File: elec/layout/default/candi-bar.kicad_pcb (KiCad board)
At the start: 2 copper layers, 85 x 25 mm, 25 parts, among them J1 ?, J10 ?, J11 ?, J12 ?, J13 ?, J14 ?, J15 ?, J16 ?, J2 ?, J3 ?, J4 ?, J5 ?, J6 ?, J7 ?, J8 ?, J9 ?, U1 ?, U2 ?, U3 ?, U4 ?, U5 ?, U6 ?, U7 ?

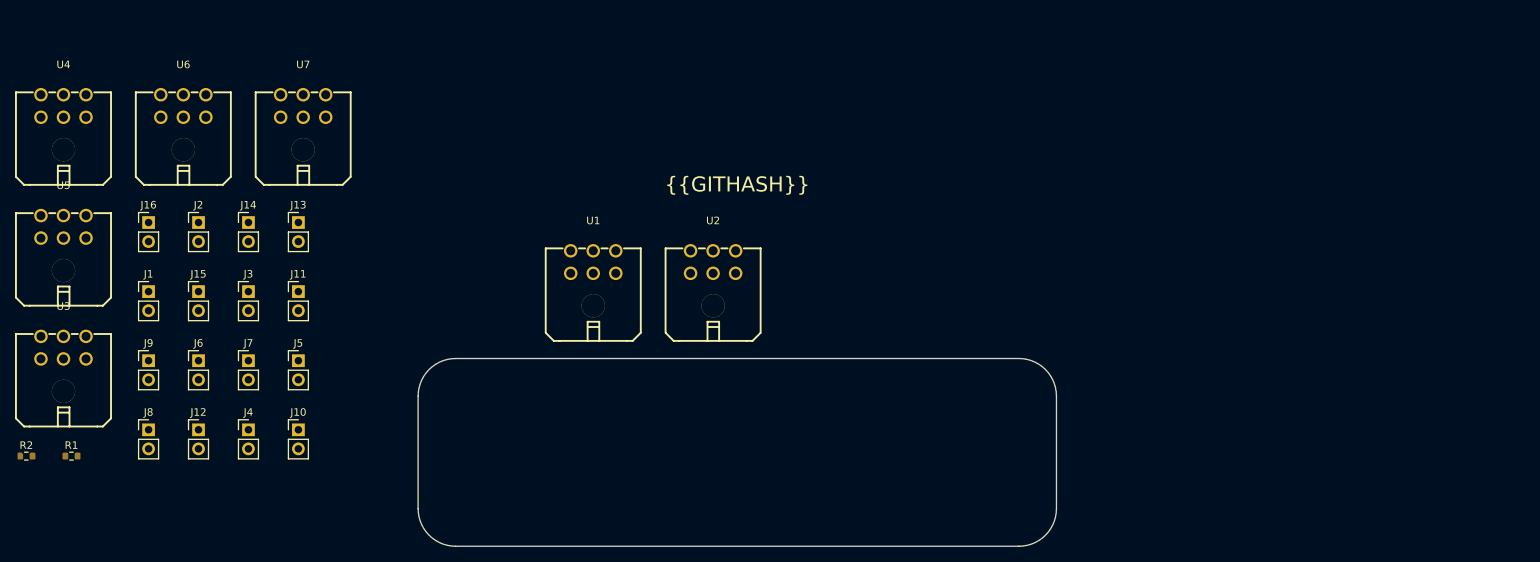
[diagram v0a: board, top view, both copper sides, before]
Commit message: feat: First revision of the CAN bus
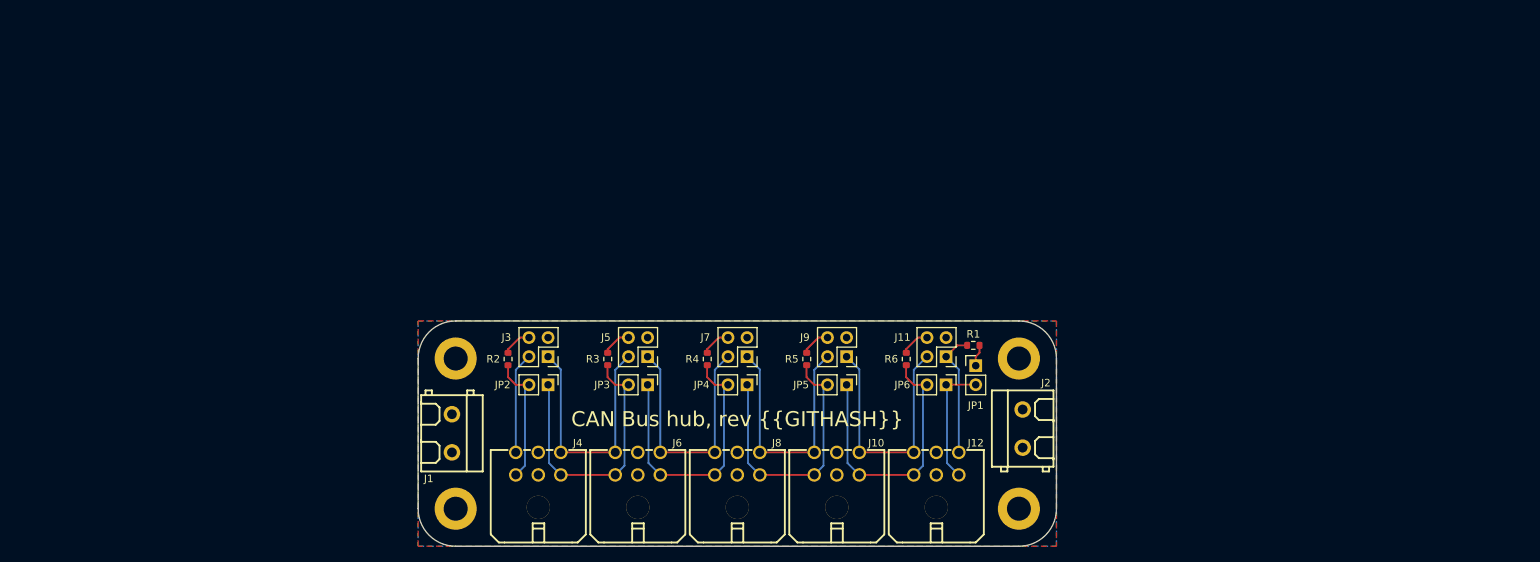
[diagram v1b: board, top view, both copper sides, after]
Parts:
- removed the J10 at (79.1, 84.5)
- removed the J12 at (65.8, 84.5)
- removed J13, J14, J15, J16: ?, lib:PinHeader_1x02_P2.54mm_Vertical
- removed the J4 at (72.4, 84.5)
- removed the J6 at (65.8, 75.3)
- removed the J8 at (59.1, 84.5)
- removed U6, U7: ?, lib:CONN-TH_43045-0600
- added JP1: ?, lib:PinHeader_1x02_P2.54mm_Vertical, F.Cu at (169.2, 76.0)
- added JP2: ?, lib:PinHeader_1x02_P2.54mm_Vertical, F.Cu at (112.3, 78.5)
- added JP3: ?, lib:PinHeader_1x02_P2.54mm_Vertical, F.Cu at (125.6, 78.5)
- added JP4: ?, lib:PinHeader_1x02_P2.54mm_Vertical, F.Cu at (138.8, 78.5)
- added JP5: ?, lib:PinHeader_1x02_P2.54mm_Vertical, F.Cu at (152.1, 78.5)
- added JP6: ?, lib:PinHeader_1x02_P2.54mm_Vertical, F.Cu at (165.3, 78.5)
- added R3: 100mW Thick Film Resistors 75V ±100ppm/℃ ±1% 120Ω 0603 Chip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, lib:R0603, F.Cu at (120.2, 75.1)
- added R4: 100mW Thick Film Resistors 75V ±100ppm/℃ ±1% 120Ω 0603 Chip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, lib:R0603, F.Cu at (133.5, 75.1)
- added R5: 100mW Thick Film Resistors 75V ±100ppm/℃ ±1% 120Ω 0603 Chip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, lib:R0603, F.Cu at (146.8, 75.1)
- added R6: 100mW Thick Film Resistors 75V ±100ppm/℃ ±1% 120Ω 0603 Chip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, lib:R0603, F.Cu at (160.0, 75.1)
- added U1: ?, lib:MountingHole_3.2mm_M3_DIN965_Pad, F.Cu at (175.0, 95.0)
- added U2: ?, lib:MountingHole_3.2mm_M3_DIN965_Pad, F.Cu at (100.0, 95.0)
- added U3: ?, lib:MountingHole_3.2mm_M3_DIN965_Pad, F.Cu at (175.0, 75.0)
- added U4: ?, lib:MountingHole_3.2mm_M3_DIN965_Pad, F.Cu at (100.0, 75.0)
- J1, J2: footprint lib:PinHeader_1x02_P2.54mm_Vertical -> lib:CONN-TH_2P-P5.08
- J11, J3, J5, J7, J9: footprint lib:PinHeader_1x02_P2.54mm_Vertical -> lib:PinHeader_2x02_P2.54mm_Vertical
- moved R1 121.0 mm to (168.9, 73.2)
- moved J12 120.4 mm to (164.0, 89.0)
- moved J10 113.5 mm to (150.8, 89.0)
- moved J2 113.1 mm to (175.5, 84.3), turned to 90 degrees
- moved J9 92.9 mm to (152.1, 74.8), turned to 180 degrees
- moved J8 91.0 mm to (137.5, 89.0)
- moved J11 86.7 mm to (165.3, 74.8), turned to 180 degrees
- moved J7 66.4 mm to (138.8, 74.8), turned to 180 degrees
- moved R2 65.4 mm to (107.0, 75.1), turned to -90 degrees
- moved J5 46.5 mm to (125.6, 74.8), turned to 180 degrees
- moved J1 44.6 mm to (99.5, 85.0), turned to -90 degrees
- moved J3 40.8 mm to (112.3, 74.8), turned to 180 degrees
- moved J6 28.7 mm to (124.2, 89.0)
- moved J4 27.8 mm to (111.0, 89.0)
- renumbered U4 to J10, U5 to J12, U1 to J4, U2 to J6, U3 to J8
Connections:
- J1 pad 1: can_term_left.sel-p1 -> gnd
- J1 pad 2: canl -> vcc
- J10 pad 1: canl-3 -> canl-4
- J10 pad 3: canl-4 -> canl-3
- J10 pad 4: canh-3 -> canh-4
- J10 pad 6: canh-4 -> canh-3
- J11 pad 1: canl-4 -> canh-5
- J11 pad 2: canl-5 -> canh-4
- J12 pad 1: canl-4 -> canl-5
- J12 pad 3: canl-5 -> canl-4
- J12 pad 4: canh-4 -> canh-5
- J12 pad 6: canh-5 -> canh-4
- J2 pad 1: can_term_right.sel-p1 -> gnd
- J2 pad 2: canl-7 -> vcc
- J3 pad 1: canl -> canh-1
- J3 pad 2: canl-1 -> canh
- J4 pad 1: canl -> canl-1
- J4 pad 3: canl-1 -> canl
- J4 pad 4: canh -> canh-1
- J4 pad 6: canh-1 -> canh
- J5 pad 1: canl-1 -> canh-2
- J5 pad 2: canl-2 -> canh-1
- J6 pad 1: canl-1 -> canl-2
- J6 pad 3: canl-2 -> canl-1
- J6 pad 4: canh-1 -> canh-2
- J6 pad 6: canh-2 -> canh-1
- J7 pad 1: canl-2 -> canh-3
- J7 pad 2: canl-3 -> canh-2
- J8 pad 1: canl-2 -> canl-3
- J8 pad 3: canl-3 -> canl-2
- J8 pad 4: canh-2 -> canh-3
- J8 pad 6: canh-3 -> canh-2
- J9 pad 1: canl-3 -> canh-4
- J9 pad 2: canl-4 -> canh-3
- R1 pad 1: canh -> canh-5
- R1 pad 2: can_term_left.sel-p1 -> p1
- R2 pad 1: canh-7 -> port_1.r_term-p4
- R2 pad 2: can_term_right.sel-p1 -> canl
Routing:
- net canl-1: track 0.00 -> 37.5 mm
- net canl-2: track 0.00 -> 37.5 mm
- net canl-4: track 0.00 -> 37.5 mm
- net canl-3: track 0.00 -> 37.5 mm
- net canh-1: track 0.00 -> 34.2 mm
- net canh-2: track 0.00 -> 34.2 mm
- net canh-4: track 0.00 -> 34.2 mm
- net canh-3: track 0.00 -> 34.2 mm
- net canl: track 0.00 -> 17.5 mm
- net canh-5: track 0.00 -> 16.9 mm
- net canl-5: track 0.00 -> 16.7 mm
- net canh: track 0.00 -> 13.5 mm
- net port_2.r_term-p4: track 0.00 -> 3.91 mm
- net port_1.r_term-p4: track 0.00 -> 3.91 mm
- net port_5.r_term-p4: track 0.00 -> 3.91 mm
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- added copper zone on B.Cu, net gnd
- added copper zone on F.Cu, net vcc
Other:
- board size 85 x 25 mm -> 85 x 30 mm
- board text added: "CAN Bus hub, rev {{GITHASH}}"
- board text removed: "{{GITHASH}}"

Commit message: feat(pcb): Minor Touchup
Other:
- board text added: "CANdiBar, rev {{GITHASH}}"
- board text removed: "CAN Bus hub, rev {{GITHASH}}"
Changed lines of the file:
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@@
 		)
 		(fp_text user "${REFERENCE}"
-			(at 0 1.27 360)
+			(at 0 1.27 0)
 			(layer "F.Fab")
 			(effects
@@
 		(at 111 89)
 		(property "Reference" "J4"
-			(at 5.25 -2.75 360)
+			(at 5.25 -2.75 0)
 			(layer "F.SilkS")
 			(effects
@@
 		)
 		(property "Value" "?"
-			(at 0 5.5 360)
+			(at 0 5.5 0)
 			(layer "F.Fab")
 			(effects
@@
 		)
 		(property "Footprint" ""
-			(at 0 0 360)
+			(at 0 0 0)
 			(layer "F.Fab")
 			(hide yes)
@@
 		)
 		(property "Datasheet" ""
-			(at 0 0 360)
+			(at 0 0 0)
 			(layer "F.Fab")
 			(hide yes)
@@
 		)
 		(property "Description" ""
-			(at 0 0 360)
+			(at 0 0 0)
 			(layer "F.Fab")
 			(hide yes)
@@
 		)
 		(fp_text user "${REFERENCE}"
-			(at 0 0 360)
+			(at 0 0 0)
 			(layer "F.Fab")
 			(effects
@@
 		(tags "mounting hole 3.2mm m3 din965")
 		(property "Reference" "U4"
-			(at 0 -3.8 360)
+			(at 0 -3.8 0)
 			(layer "F.SilkS")
 			(hide yes)
@@
 		)
 		(property "Value" "?"
-			(at 0 3.8 360)
+			(at 0 3.8 0)
 			(layer "F.Fab")
 			(effects
@@
 		)
 		(fp_text user "${REFERENCE}"
-			(at 0 0 360)
+			(at 0 0 0)
 			(layer "F.Fab")
 			(effects
@@
 		(tags "mounting hole 3.2mm m3 din965")
 		(property "Reference" "U1"
-			(at 0 -3.8 360)
+			(at 0 -3.8 0)
 			(layer "F.SilkS")
 			(hide yes)
@@
 		)
 		(property "Value" "?"
-			(at 0 3.8 360)
+			(at 0 3.8 0)
 			(layer "F.Fab")
 			(effects
@@
 		)
 		(fp_text user "${REFERENCE}"
-			(at 0 0 360)
+			(at 0 0 0)
 			(layer "F.Fab")
 			(effects
@@
 		(tags "Through hole pin header THT 2x02 2.54mm double row")
 		(property "Reference" "J9"
-			(at 5.5525 2.57 360)
+			(at 5.5525 2.57 0)
 			(layer "F.SilkS")
 			(effects
@@
 		)
 		(property "Value" "?"
-			(at 1.27 4.87 360)
+			(at 1.27 4.87 0)
 			(layer "F.Fab")
 			(effects
@@
 		(tags "Through hole pin header THT 2x02 2.54mm double row")
 		(property "Reference" "J3"
-			(at 5.5525 2.57 360)
+			(at 5.5525 2.57 0)
 			(layer "F.SilkS")
 			(effects
@@
 		)
 		(property "Value" "?"
-			(at 1.27 4.87 360)
+			(at 1.27 4.87 0)
 			(layer "F.Fab")
 			(effects
@@
 		(tags "Through hole pin header THT 1x02 2.54mm single row")
 		(property "Reference" "JP1"
-			(at 0 5.3 360)
+			(at 0 5.3 0)
 			(layer "F.SilkS")
 			(effects
@@
 		)
 		(property "Value" "?"
-			(at 0 4.87 360)
+			(at 0 4.87 0)
 			(layer "F.Fab")
 			(effects
@@
 		(tags "mounting hole 3.2mm m3 din965")
 		(property "Reference" "U2"
-			(at 0 -3.8 360)
+			(at 0 -3.8 0)
 			(layer "F.SilkS")
 			(hide yes)
@@
 		)
 		(property "Value" "?"
-			(at 0 3.8 360)
+			(at 0 3.8 0)
 			(layer "F.Fab")
 			(effects
@@
 		)
 		(fp_text user "${REFERENCE}"
-			(at 0 0 360)
+			(at 0 0 0)
 			(layer "F.Fab")
 			(effects
@@
 		(at 164 89)
 		(property "Reference" "J12"
-			(at 5.25 -2.75 360)
+			(at 5.25 -2.75 0)
 			(layer "F.SilkS")
 			(effects
@@
 		)
 		(property "Value" "?"
-			(at 0 5.5 360)
+			(at 0 5.5 0)
 			(layer "F.Fab")
 			(effects
@@
 		)
 		(property "Footprint" ""
-			(at 0 0 360)
+			(at 0 0 0)
 			(layer "F.Fab")
 			(hide yes)
@@
 		)
 		(property "Datasheet" ""
-			(at 0 0 360)
+			(at 0 0 0)
 			(layer "F.Fab")
 			(hide yes)
@@
 		)
 		(property "Description" ""
-			(at 0 0 360)
+			(at 0 0 0)
 			(layer "F.Fab")
 			(hide yes)
@@
 		)
 		(fp_text user "${REFERENCE}"
-			(at 0 0 360)
+			(at 0 0 0)
 			(layer "F.Fab")
 			(effects
@@
 		(tags "mounting hole 3.2mm m3 din965")
 		(property "Reference" "U3"
-			(at 0 -3.8 360)
+			(at 0 -3.8 0)
 			(layer "F.SilkS")
 			(hide yes)
@@
 		)
 		(property "Value" "?"
-			(at 0 3.8 360)
+			(at 0 3.8 0)
 			(layer "F.Fab")
 			(effects
@@
 		)
 		(fp_text user "${REFERENCE}"
-			(at 0 0 360)
+			(at 0 0 0)
 			(layer "F.Fab")
 			(effects
@@
 		(tags "Through hole pin header THT 2x02 2.54mm double row")
 		(property "Reference" "J7"
-			(at 5.5525 2.57 360)
+			(at 5.5525 2.57 0)
 			(layer "F.SilkS")
 			(effects
@@
 		)
 		(property "Value" "?"
-			(at 1.27 4.87 360)
+			(at 1.27 4.87 0)
 			(layer "F.Fab")
 			(effects
@@
 		(at 150.75 89)
 		(property "Reference" "J10"
-			(at 5.25 -2.75 360)
+			(at 5.25 -2.75 0)
 			(layer "F.SilkS")
 			(effects
@@
 		)
 		(property "Value" "?"
-			(at 0 5.5 360)
+			(at 0 5.5 0)
 			(layer "F.Fab")
 			(effects
@@
 		)
 		(property "Footprint" "lib:CONN-TH_43045-0600"
-			(at 0 0 360)
+			(at 0 0 0)
 			(layer "F.Fab")
 			(hide yes)
@@
 		)
 		(property "Datasheet" ""
-			(at 0 0 360)
+			(at 0 0 0)
 			(layer "F.Fab")
 			(hide yes)
@@
 		)
 		(property "Description" ""
-			(at 0 0 360)
+			(at 0 0 0)
 			(layer "F.Fab")
 			(hide yes)
@@
 		)
 		(fp_text user "${REFERENCE}"
-			(at 0 0 360)
+			(at 0 0 0)
 			(layer "F.Fab")
 			(effects
@@
 		(tags "Through hole pin header THT 2x02 2.54mm double row")
 		(property "Reference" "J11"
-			(at 5.8025 2.57 360)
+			(at 5.8025 2.57 0)
 			(layer "F.SilkS")
 			(effects
@@
 		)
 		(property "Value" "?"
-			(at 1.27 4.87 360)
+			(at 1.27 4.87 0)
 			(layer "F.Fab")
 			(effects
@@
 		)
 		(fp_text user "${REFERENCE}"
-			(at 0 1.27 360)
+			(at 0 1.27 0)
 			(layer "F.Fab")
 			(effects
@@
 		(at 137.5 89)
 		(property "Reference" "J8"
-			(at 5.25 -2.75 360)
+			(at 5.25 -2.75 0)
 			(layer "F.SilkS")
 			(effects
@@
 		)
 		(property "Value" "?"
-			(at 0 5.5 360)
+			(at 0 5.5 0)
 			(layer "F.Fab")
 			(effects
@@
 		)
 		(property "Footprint" ""
-			(at 0 0 360)
+			(at 0 0 0)
 			(layer "F.Fab")
 			(hide yes)
@@
 		)
 		(property "Datasheet" ""
-			(at 0 0 360)
+			(at 0 0 0)
 			(layer "F.Fab")
 			(hide yes)
@@
 		)
 		(property "Description" ""
-			(at 0 0 360)
+			(at 0 0 0)
 			(layer "F.Fab")
 			(hide yes)
@@
 		)
 		(fp_text user "${REFERENCE}"
-			(at 0 0 360)
+			(at 0 0 0)
 			(layer "F.Fab")
 			(effects
@@
 		)
 		(fp_text user "${REFERENCE}"
-			(at 0 1.27 360)
+			(at 0 1.27 0)
 			(layer "F.Fab")
 			(effects
@@
 		)
 		(fp_text user "${REFERENCE}"
-			(at 0 1.27 360)
+			(at 0 1.27 0)
 			(layer "F.Fab")
 			(effects
@@
 		(tags "Through hole pin header THT 2x02 2.54mm double row")
 		(property "Reference" "J5"
-			(at 5.5525 2.57 360)
+			(at 5.5525 2.57 0)
 			(layer "F.SilkS")
 			(effects
@@
 		)
 		(property "Value" "?"
-			(at 1.27 4.87 360)
+			(at 1.27 4.87 0)
 			(layer "F.Fab")
 			(effects
@@
 		)
 		(fp_text user "${REFERENCE}"
-			(at 0 1.27 360)
+			(at 0 1.27 0)
 			(layer "F.Fab")
 			(effects
@@
 		(at 124.25 89)
 		(property "Reference" "J6"
-			(at 5.25 -2.75 360)
+			(at 5.25 -2.75 0)
 			(layer "F.SilkS")
 			(effects
@@
 		)
 		(property "Value" "?"
-			(at 0 5.5 360)
+			(at 0 5.5 0)
 			(layer "F.Fab")
 			(effects
@@
 		)
 		(property "Footprint" ""
-			(at 0 0 360)
+			(at 0 0 0)
 			(layer "F.Fab")
 			(hide yes)
@@
 		)
 		(property "Datasheet" ""
-			(at 0 0 360)
+			(at 0 0 0)
 			(layer "F.Fab")
 			(hide yes)
@@
 		)
 		(property "Description" ""
-			(at 0 0 360)
+			(at 0 0 0)
 			(layer "F.Fab")
 			(hide yes)
@@
 		)
 		(fp_text user "${REFERENCE}"
-			(at 0 0 360)
+			(at 0 0 0)
 			(layer "F.Fab")
 			(effects
@@
 		(layer "Edge.Cuts")
 	)
-	(gr_text "CAN Bus hub, rev {{GITHASH}}"
+	(gr_text "CANdiBar, rev {{GITHASH}}"
 		(at 137.5 84.25 0)
 		(layer "F.SilkS")
